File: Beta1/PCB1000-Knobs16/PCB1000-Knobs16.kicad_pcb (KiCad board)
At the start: 2 copper layers, 188.9 x 30.9 mm, 39 parts, among them U1000 MCP3008T-I/SL, U2 MCP3008T-I/SL

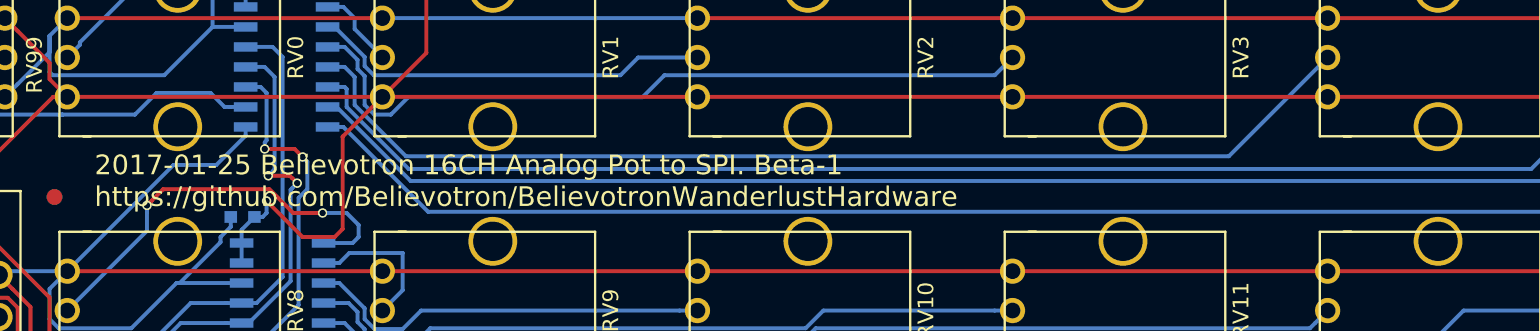
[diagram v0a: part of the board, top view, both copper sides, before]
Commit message: Renamed to Knobs16. Updated PCB Silk
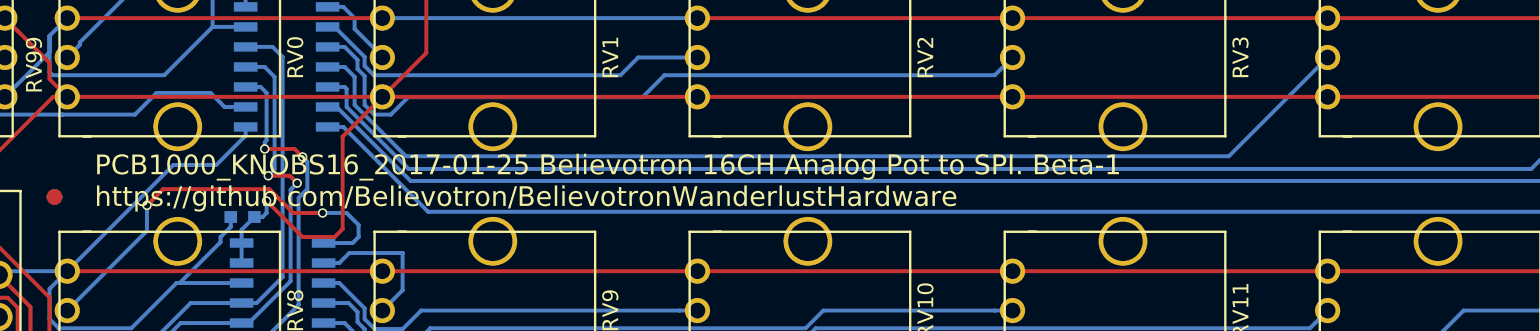
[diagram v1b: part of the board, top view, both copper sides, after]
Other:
- board text added: "PCB1000_KNOBS16_2017-01-25 Believotron 16CH Analog Pot to SPI. Beta-1 https://github.com/Believotron/BelievotronWanderlustHardware"
- board text removed: "2017-01-25 Believotron 16CH Analog Pot to SPI. Beta-1 https://github.com/Believotron/BelievotronWanderlustHardware"
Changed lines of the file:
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@@
   (general
     (links 86)
-    (no_connects 1)
+    (no_connects 0)
     (area 0 -33.148 193.960001 1.255473)
     (thickness 1.6)
@@
     (effects (font (size 1.5 1.5) (thickness 0.3)))
   )
-  (gr_text "2017-01-25 Believotron 16CH Analog Pot to SPI. Beta-1\nhttps://github.com/Believotron/BelievotronWanderlustHardware\n" (at 30.48 -16.256) (layer F.SilkS)
+  (gr_text "PCB1000_KNOBS16_2017-01-25 Believotron 16CH Analog Pot to SPI. Beta-1\nhttps://github.com/Believotron/BelievotronWanderlustHardware\n" (at 30.48 -16.256) (layer F.SilkS)
     (effects (font (size 1.25 1.25) (thickness 0.25)) (justify left))
   )

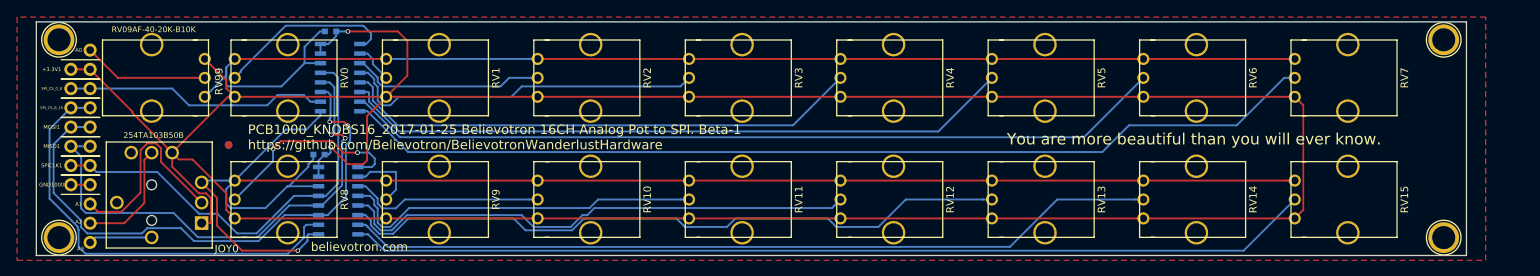
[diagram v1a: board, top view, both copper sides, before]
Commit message: Moved input connector to avoid interference w screw
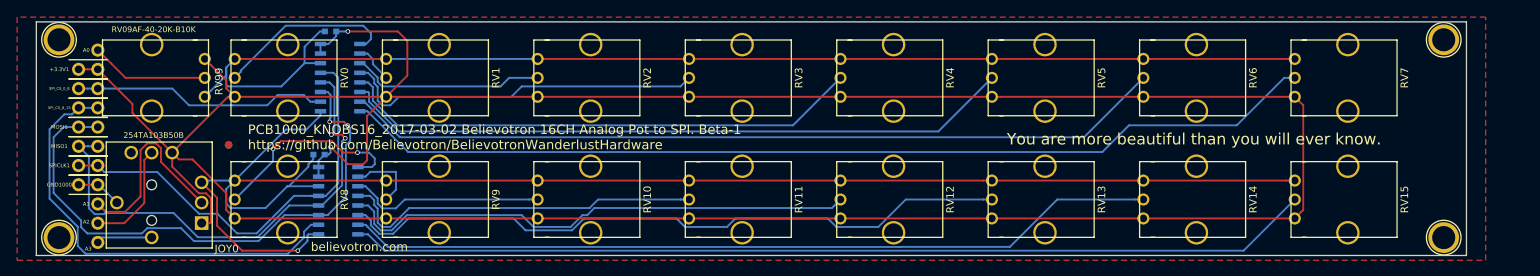
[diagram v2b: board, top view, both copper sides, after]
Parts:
- moved +3.3V1 1.02 mm to (8.13, -25.2)
- moved A0 1.02 mm to (10.7, -27.8)
- moved A1 1.02 mm to (10.7, -7.44)
- moved A2 1.02 mm to (10.7, -4.90)
- moved A3 1.02 mm to (10.7, -2.36)
- moved GND1000 1.02 mm to (8.13, -9.98)
- moved MISO1 1.02 mm to (8.13, -15.1)
- moved MOSI1 1.02 mm to (8.13, -17.6)
- moved SPICLK1 1.02 mm to (8.13, -12.5)
- moved SPI_CS_0_8 1.02 mm to (8.13, -22.7)
- moved SPI_CS_8_15 1.02 mm to (8.13, -20.1)
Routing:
- net GND: track 377.8 -> 381.3 mm
- net /MOSI: track 74.4 -> 76.0 mm
- net Net-(A2-Pad1): track 15.3 -> 14.3 mm
- net /SPICLK: track 58.3 -> 57.3 mm
- net /CS_R0_7: track 35.1 -> 34.0 mm
- net /VOLUME: track 16.7 -> 15.6 mm
- net /MISO: track 67.1 -> 66.2 mm
- net Net-(A1-Pad1): track 26.5 -> 25.8 mm
- net /CS_LED_8_15: track 58.1 -> 58.8 mm
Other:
- board text added: "PCB1000_KNOBS16_2017-03-02 Believotron 16CH Analog Pot to SPI. Beta-1 https://github.com/Believotron/BelievotronWanderlustHardware"
- board text removed: "PCB1000_KNOBS16_2017-01-25 Believotron 16CH Analog Pot to SPI. Beta-1 https://github.com/Believotron/BelievotronWanderlustHardware"

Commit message: Increased width by 2U. Ready for FAB
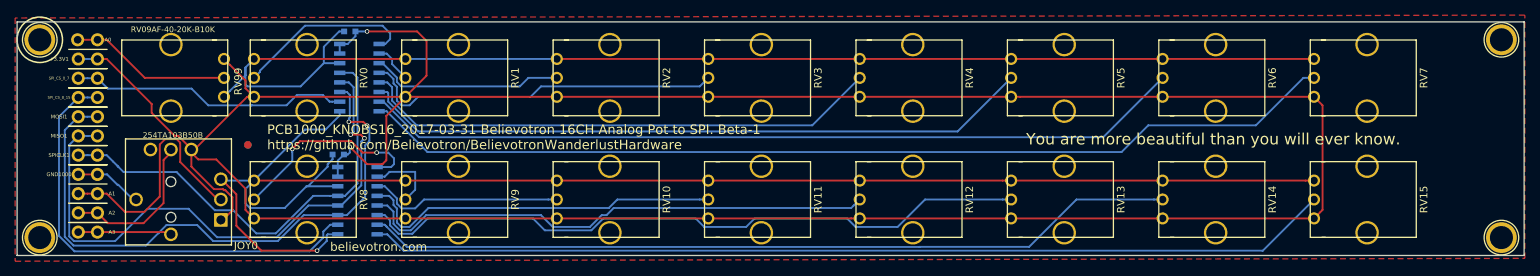
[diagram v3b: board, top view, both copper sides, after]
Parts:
- added A0: CONN_01X01, Liberry:single_0.1, F.Cu at (8.00, -29.1)
- added A1: CONN_01X01, Liberry:single_0.1, F.Cu at (8.08, -8.80)
- added A2: CONN_01X01, Liberry:single_0.1, F.Cu at (8.08, -6.26)
- added A3: CONN_01X01, Liberry:single_0.1, F.Cu at (8.08, -3.73)
- moved REF** 7.62 mm to (196.0, -29.1)
- moved REF** 7.62 mm to (196.0, -3.00)
- moved JOY0 2.57 mm to (20.3, -8.03)
- moved RV13 2.54 mm to (138.3, -8.03)
- moved RV14 2.54 mm to (158.3, -8.03)
- moved RV15 2.54 mm to (178.3, -8.03)
- moved RV5 2.54 mm to (138.3, -24.1)
- moved RV6 2.54 mm to (158.3, -24.1)
- moved RV7 2.54 mm to (178.3, -24.1)
- moved U1000 2.54 mm to (45.2, -24.1)
- moved REF** 2.54 mm to (3.00, -3.00)
- moved REF** 2.54 mm to (3.00, -29.1)
- moved C1000 2.54 mm to (43.9, -30.2)
- moved C2 2.54 mm to (42.4, -14.0)
- moved REF** 2.54 mm to (30.5, -15.2)
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- renumbered SPI_CS_0_8 to SPI_CS_0_7
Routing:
- net /MISO: track 66.2 -> 78.3 mm
- net Net-(A1-Pad1): track 25.8 -> 32.8 mm
- net /VOLUME: track 15.6 -> 21.4 mm
- net Net-(A2-Pad1): track 14.3 -> 20.0 mm
- net /MOSI: track 76.0 -> 81.3 mm
- net Net-(A3-Pad1): track 8.40 -> 12.4 mm
- net +3V3: track 403.2 -> 406.8 mm
- net /SPICLK: track 57.3 -> 60.7 mm
- net /CS_R0_7: track 34.0 -> 37.2 mm
- net GND: track 381.3 -> 384.2 mm
- net /CS_LED_8_15: track 58.8 -> 61.4 mm
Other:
- board size 188.9 x 30.9 mm -> 199 x 30.9 mm
- board text added: "(Bottom Row) SPI_CS_8_15"
- board text added: "(Data In) MOSI"
- board text added: "(Data Out) MISO"
- board text added: "(Joy Button) A3"
- board text added: "(Joy X) A2"
- board text added: "(Joy Y) A1"
- board text added: "(Top Row) SPI_CS_0_7"
- board text added: "(Volume) A0"
- board text added: "+3.3V"
- board text added: "0.1 uF"
- board text added: "GND"
- board text added: "Marketing pap: Believotron.com The good stuff: community.believotron.com"
- board text added: "NO: Req ext / micro pullup Button push connects to GND."
- board text added: "PCB1000_KNOBS16_2017-03-31 Believotron 16CH Analog Pot to SPI. Beta-1 https://github.com/Believotron/BelievotronWanderlustHardware"
- board text added: "SPICLK"
- board text removed: "PCB1000_KNOBS16_2017-03-02 Believotron 16CH Analog Pot to SPI. Beta-1 https://github.com/Believotron/BelievotronWanderlustHardware"

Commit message: Updated Flavor Text. Ready for Fab
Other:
- board text added: "Open source MIT license files at: github.com/Believotron/BelievotronWanderlustHardware Replacement parts, upgrades, updates, new gear, and marketing pap: Believotron.com For help, bug reporting, dev-blogs, or joy at your bonkers-cool creation, the good stuff is here: community.believotron.com"
- board text removed: "Marketing pap: Believotron.com The good stuff: community.believotron.com"
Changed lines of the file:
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@@
       (net 26 "Net-(A3-Pad1)"))
   )
-  (gr_text "Marketing pap: Believotron.com\nThe good stuff: community.believotron.com" (at 196.04 -24.045) (layer B.SilkS)
+  (gr_text "Open source MIT license files at: github.com/Believotron/BelievotronWanderlustHardware\nReplacement parts, upgrades, updates, new gear, and marketing pap: Believotron.com\nFor help, bug reporting, dev-blogs, or joy at your bonkers-cool creation, the good stuff is here: community.believotron.com\n" (at 196.04 -24.045) (layer B.SilkS)
     (effects (font (size 0.6 0.6) (thickness 0.15)) (justify left mirror))
   )
